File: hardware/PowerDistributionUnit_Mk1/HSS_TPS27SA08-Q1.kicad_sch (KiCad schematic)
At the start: 29 parts, among them U3 TPS27SA08CQPWPRQ1, U32 ACS37042KLHBLT-010B3

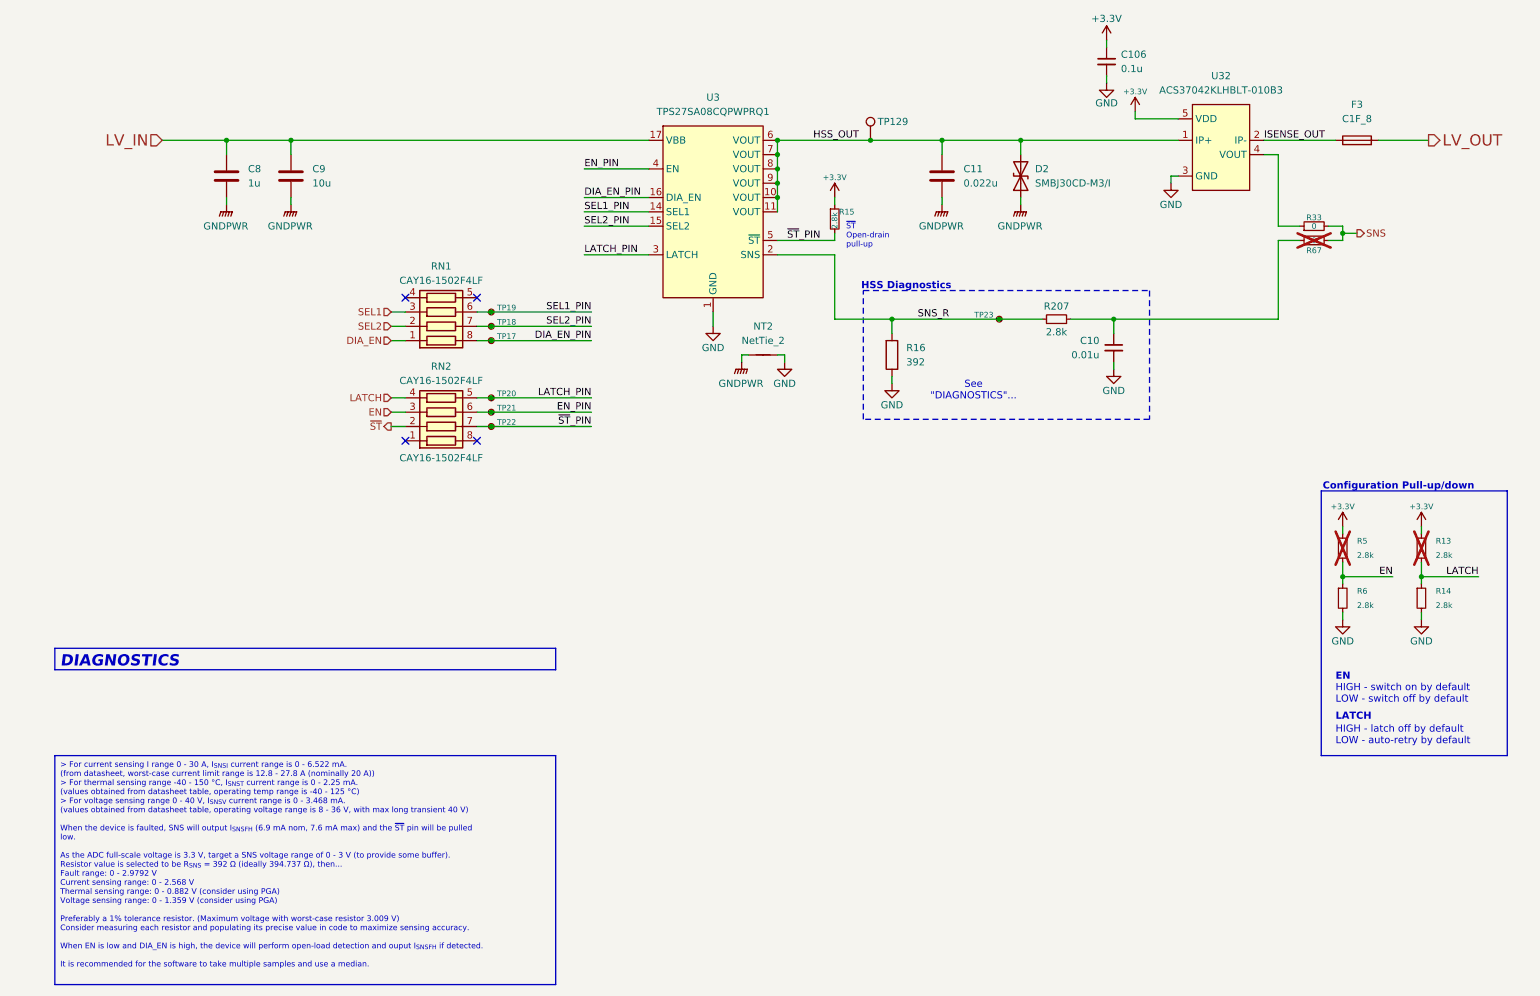
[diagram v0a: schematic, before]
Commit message: update schematic documentation, clean up, update titleblocks
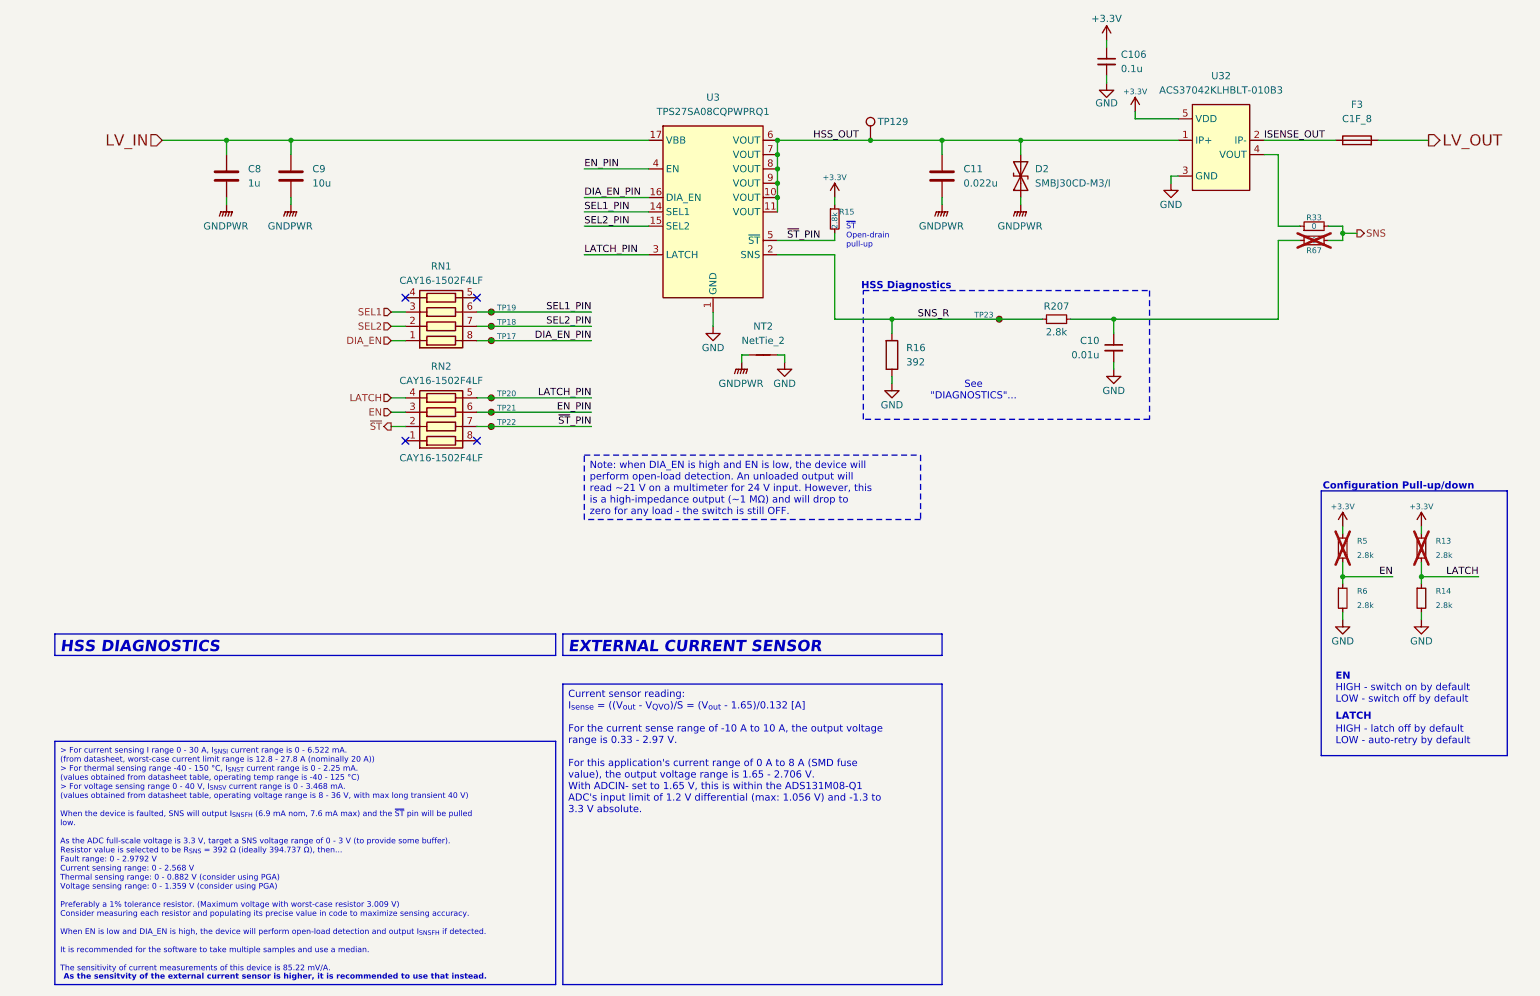
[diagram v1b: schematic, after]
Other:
- note added: "As the sensitvity of the external current sensor is higher, it is recommended to use that instead."
